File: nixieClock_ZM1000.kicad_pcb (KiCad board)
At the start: 2 copper layers, 142.2 x 88.5 mm, 71 parts, among them J1 Conn_01x03_Female, J2 Conn_01x02_Female, Q1 BC547, Q2 BC547, Q3 BC547, Q4 BC547, Q5 BC547, Q6 BC547, Q7 Q_NMOS_GDS, T1 Transformer_1P_1S, U1 WeMos_mini, U10 ZM1000, U11 SN74141, U12 SN74141, U13 SN74141, U14 74HC595, U15 74HC595, U16 74HC595, U17 74HC595, U18 LM3478, U19 BME280, U2 ZM1000, U3 ZM1000, U4 ZM1000, U5 SN74141, U6 SN74141, U7 SN74141, U8 ZM1000, U9 ZM1000

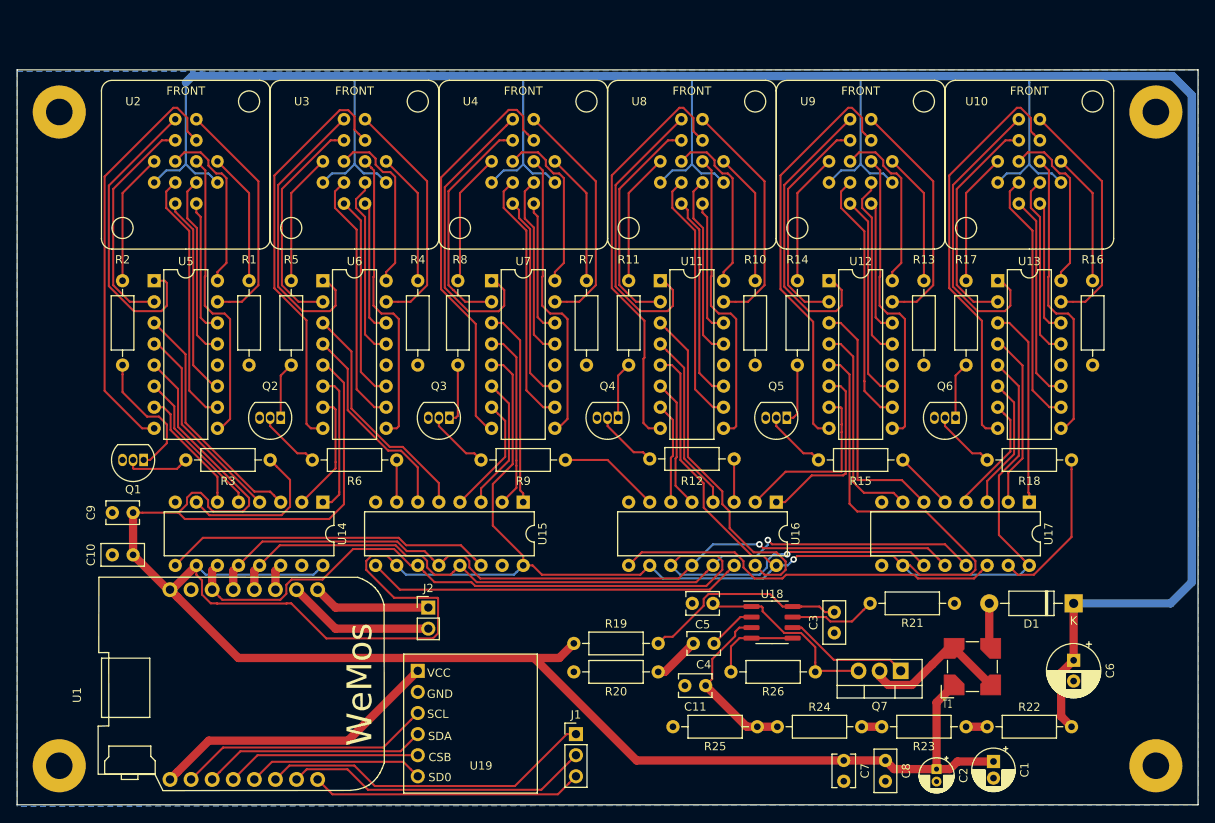
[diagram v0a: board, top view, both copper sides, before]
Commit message: Fixed tube footprints and rerouted
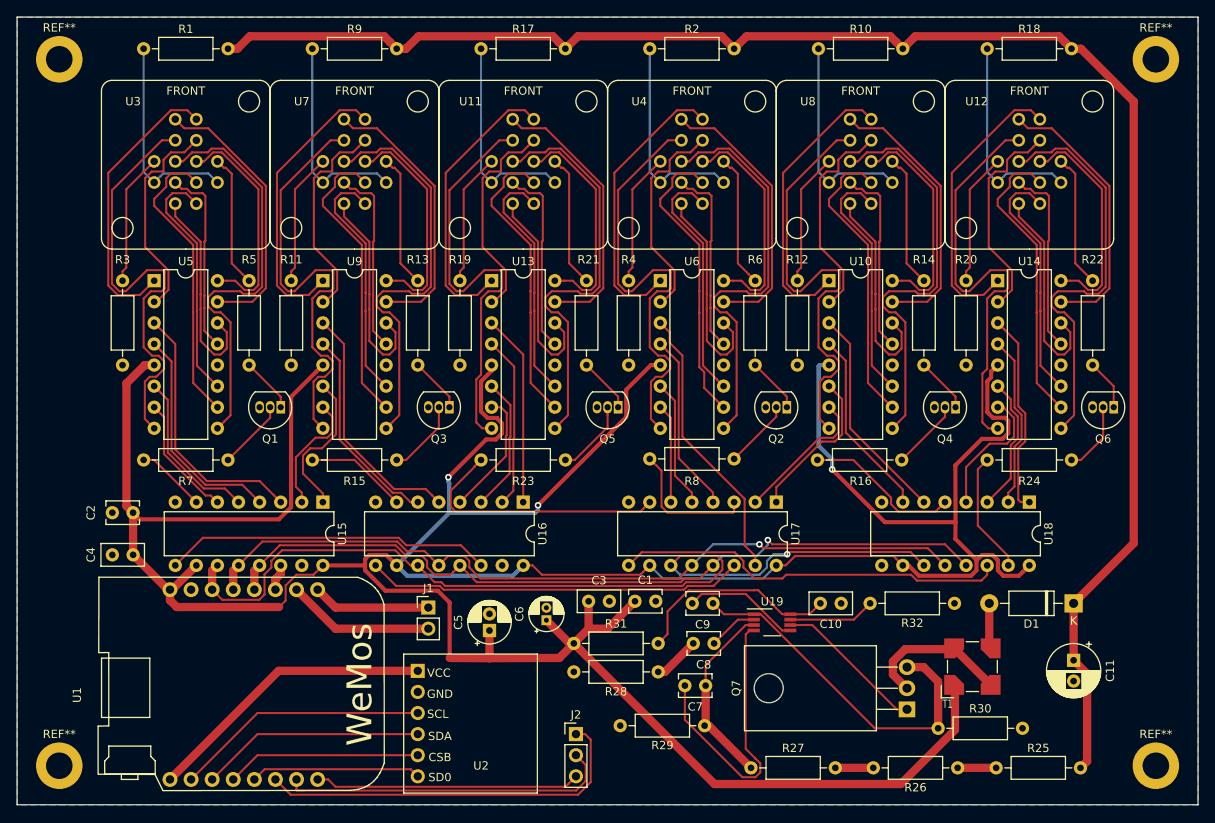
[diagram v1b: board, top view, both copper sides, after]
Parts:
- removed the Q3 at (120.7, 88.9)
- removed the Q4 at (141.0, 88.9)
- removed the R23 at (182.9, 126.1)
- removed the R6 at (104.1, 94.0)
- removed the REF** at (73.7, 130.8)
- removed the REF** at (205.7, 130.8)
- removed the REF** at (73.7, 52.1)
- removed the REF** at (205.7, 52.1)
- removed the U18 at (159.5, 113.5)
- added Q2: BC547, Package_TO_SOT_THT:TO-92_Inline, F.Cu at (161.3, 87.6)
- added Q5: BC547, Package_TO_SOT_THT:TO-92_Inline, F.Cu at (141.0, 87.6)
- added R10: 20k, Resistor_THT:R_Axial_DIN0207_L6.3mm_D2.5mm_P10.16mm_Horizontal, F.Cu at (165.1, 44.5)
- added R15: 10k, Resistor_THT:R_Axial_DIN0207_L6.3mm_D2.5mm_P10.16mm_Horizontal, F.Cu at (114.3, 94.0)
- added R17: 20k, Resistor_THT:R_Axial_DIN0207_L6.3mm_D2.5mm_P10.16mm_Horizontal, F.Cu at (124.5, 44.5)
- added R18: 20k, Resistor_THT:R_Axial_DIN0207_L6.3mm_D2.5mm_P10.16mm_Horizontal, F.Cu at (185.4, 44.5)
- added R2: 20k, Resistor_THT:R_Axial_DIN0207_L6.3mm_D2.5mm_P10.16mm_Horizontal, F.Cu at (144.8, 44.5)
- added R26: 820k, Resistor_THT:R_Axial_DIN0207_L6.3mm_D2.5mm_P10.16mm_Horizontal, F.Cu at (181.9, 131.1)
- added R7: 10k, Resistor_THT:R_Axial_DIN0207_L6.3mm_D2.5mm_P10.16mm_Horizontal, F.Cu at (94.0, 94.0)
- added R9: 20k, Resistor_THT:R_Axial_DIN0207_L6.3mm_D2.5mm_P10.16mm_Horizontal, F.Cu at (104.1, 44.5)
- added REF**: MountingHole_3.2mm_M3_DIN965_Pad, MountingHole:MountingHole_3.2mm_M3_DIN965_Pad, F.Cu at (205.7, 130.8)
- added REF**: MountingHole_3.2mm_M3_DIN965_Pad, MountingHole:MountingHole_3.2mm_M3_DIN965_Pad, F.Cu at (205.7, 45.7)
- added REF**: MountingHole_3.2mm_M3_DIN965_Pad, MountingHole:MountingHole_3.2mm_M3_DIN965_Pad, F.Cu at (73.7, 45.7)
- added REF**: MountingHole_3.2mm_M3_DIN965_Pad, MountingHole:MountingHole_3.2mm_M3_DIN965_Pad, F.Cu at (73.7, 130.8)
- added U19: LM3478, Package_SO:VSSOP-8_3.0x3.0mm_P0.65mm, F.Cu at (159.5, 113.5)
- Q7: footprint Package_TO_SOT_THT:TO-220-3_Vertical -> Package_TO_SOT_THT:TO-220-3_Horizontal_TabDown
- R1: value 10M -> 20k
- R3: value 10k -> 10M
- T1: footprint BamboulabFootprints:Transformer_LPR6235 -> Bamboulibs:Transformer_LPR6235
- U1: footprint BamboulabFootprints:D1_mini_board -> Bamboulibs:D1_mini_board
- moved C5 62.7 mm to (125.5, 114.5), turned to 90 degrees
- moved C6 50.3 mm to (132.3, 113.3), turned to 90 degrees
- moved C3 40.6 mm to (137.4, 111.0), turned to 0 degrees
- moved C1 31.6 mm to (143.0, 111.0), turned to 0 degrees
- moved R1 30.7 mm to (83.8, 44.5), turned to 0 degrees
- moved R3 22.9 mm to (81.3, 72.4), turned to 270 degrees
- moved Q4 20.4 mm to (181.6, 87.6)
- moved Q3 20.4 mm to (120.7, 87.6)
- moved Q6 19.1 mm to (200.7, 87.6)
- moved Q1 17.7 mm to (100.3, 87.6)
- moved R30 16.3 mm to (179.5, 126.3), turned to 0 degrees
- moved R21 15.5 mm to (137.2, 82.5)
- moved R11 15.2 mm to (101.6, 72.4)
- moved R12 15.2 mm to (162.6, 72.4)
- moved R13 15.2 mm to (116.8, 82.5)
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- renumbered C7 to C1, C3 to C10, C6 to C11, C9 to C2, C8 to C3, C10 to C4, C1 to C5, C2 to C6, C11 to C7, C4 to C8, C5 to C9, J2 to J1, J1 to J2, Q2 to Q3, Q5 to Q4, R4 to R11, R13 to R12, R5 to R13, R15 to R16, R7 to R19, R16 to R20, R8 to R21, R17 to R22, R9 to R23, R18 to R24, R22 to R25, R24 to R27, R20 to R28, R25 to R29, R26 to R30, R19 to R31, R21 to R32, R10 to R4, R2 to R5, R11 to R6, R12 to R8, U12 to U10, U4 to U11, U10 to U12, U7 to U13, U13 to U14, U14 to U15, U15 to U16, U16 to U17, U17 to U18, U19 to U2, U2 to U3, U8 to U4, U11 to U6, U3 to U7, U9 to U8, U6 to U9
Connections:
- R1 pad 2: GND -> /PSU/HV
- R3 pad 1: Net-(Q1-Pad2) -> Net-(R3-Pad1)
- R3 pad 2: /Shift Registers/DP1 -> GND
- U11 pad 1: /PSU/HV -> Net-(R17-Pad1)
- U11 pad 2: /PSU/HV -> Net-(R17-Pad1)
- U12 pad 1: /PSU/HV -> Net-(R18-Pad1)
- U12 pad 2: /PSU/HV -> Net-(R18-Pad1)
- U3 pad 1: /PSU/HV -> Net-(R1-Pad1)
- U3 pad 14: Net-(R1-Pad1) -> Net-(R3-Pad1)
- U3 pad 2: /PSU/HV -> Net-(R1-Pad1)
- U4 pad 1: /PSU/HV -> Net-(R2-Pad1)
- U4 pad 2: /PSU/HV -> Net-(R2-Pad1)
- U7 pad 1: /PSU/HV -> Net-(R9-Pad1)
- U7 pad 2: /PSU/HV -> Net-(R9-Pad1)
- U8 pad 1: /PSU/HV -> Net-(R10-Pad1)
- U8 pad 2: /PSU/HV -> Net-(R10-Pad1)
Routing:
- net /PSU/HV: track 333.3 -> 202.2 mm
- net /Control/5V: track 505.5 -> 439.4 mm, vias 1 -> 3
- net GND: track 10.9 -> 48.9 mm
- net Net-(R10-Pad1): track 0.00 -> 25.2 mm
- net Net-(R18-Pad1): track 0.00 -> 25.2 mm
- net Net-(R9-Pad1): track 0.00 -> 25.2 mm
- net Net-(R17-Pad1): track 0.00 -> 25.2 mm
- net Net-(R2-Pad1): track 0.00 -> 25.2 mm
- net Net-(C9-Pad1): track 22.5 -> 43.4 mm
- net /Shift Registers/DP3: track 12.3 -> 31.8 mm
- net Net-(R3-Pad1): track 0.00 -> 15.9 mm
- net Net-(U11-Pad6): track 35.6 -> 50.3 mm
- net Net-(U3-Pad6): track 35.6 -> 50.3 mm
- net Net-(U12-Pad6): track 35.6 -> 50.3 mm
- net Net-(U7-Pad6): track 36.1 -> 50.3 mm
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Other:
- board size 142.2 x 88.5 mm -> 142.2 x 94.9 mm
